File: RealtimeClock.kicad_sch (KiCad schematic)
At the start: 6 parts, among them U21 74HC02, U22 DS12885+, Y2 32.768kHz

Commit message: Schematic cleanup
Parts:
- removed unit 5 of U21
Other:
- moved on the sheet: U21A, U21B, U21C

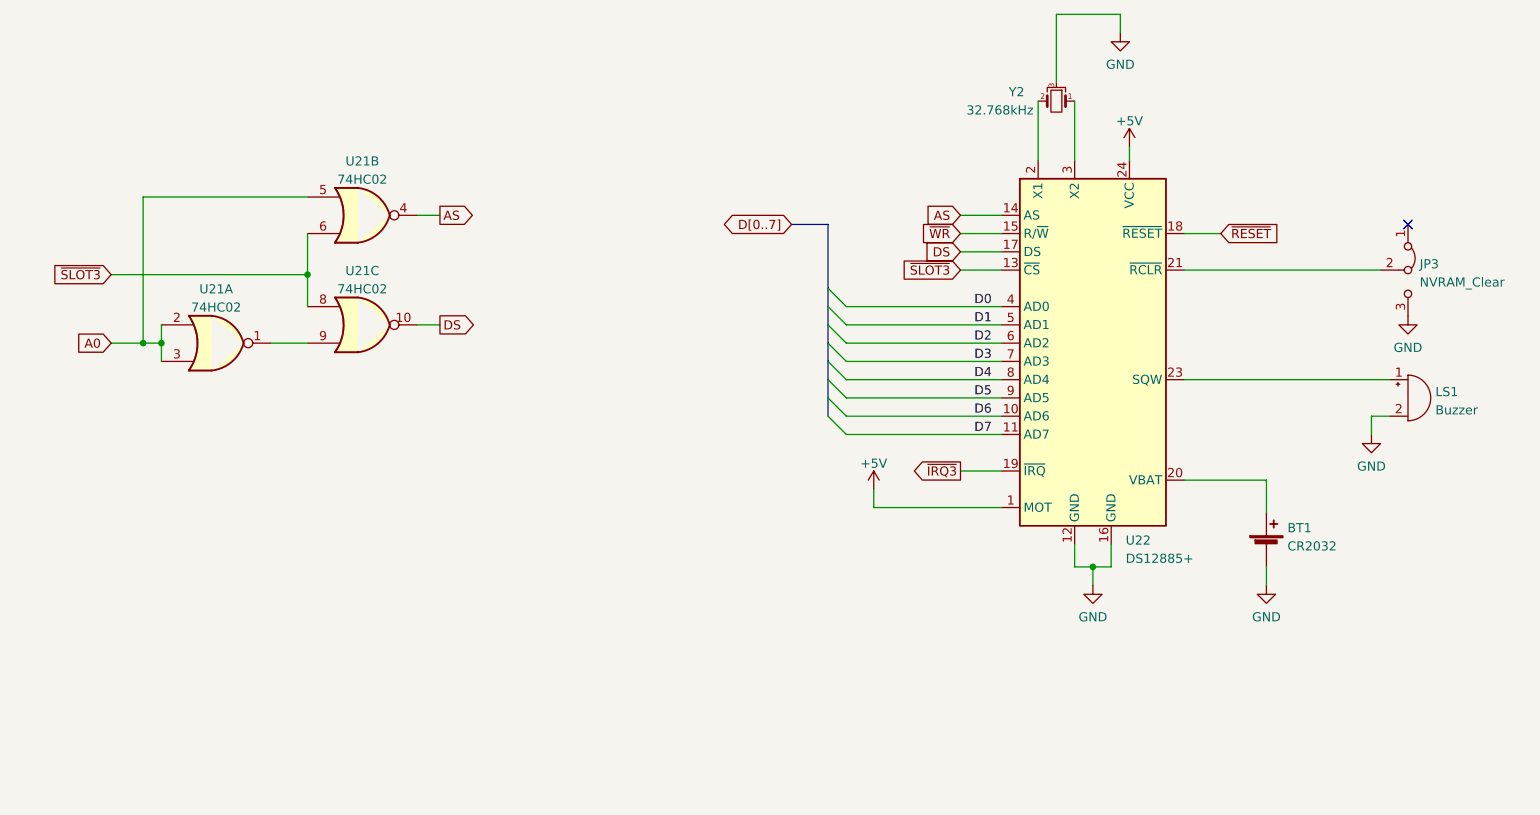
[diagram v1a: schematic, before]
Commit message: Memory expansion moved to low memory
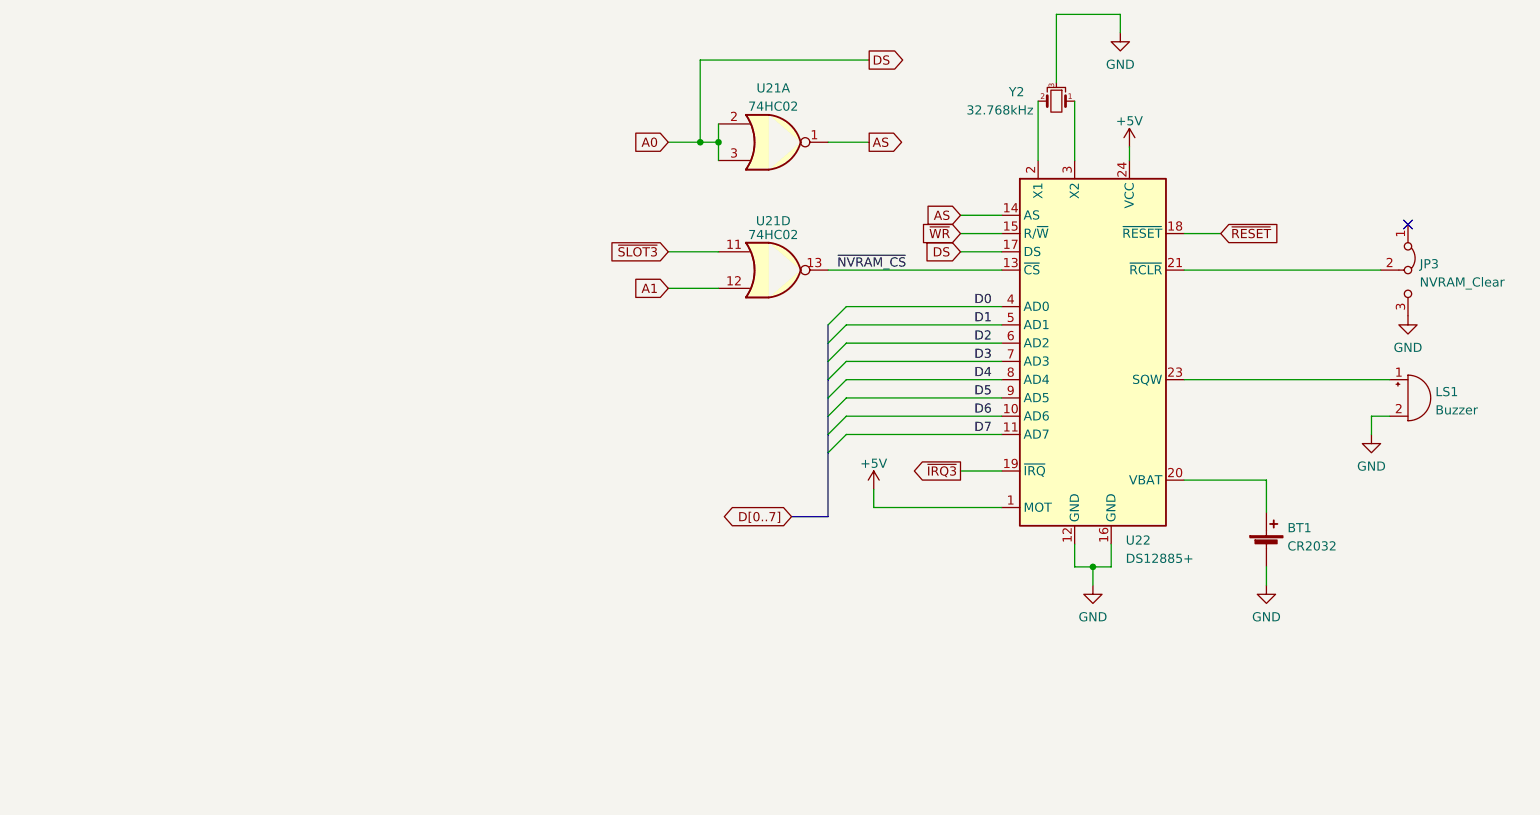
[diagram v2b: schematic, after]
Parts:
- removed unit 3 of U21
- removed unit 2 of U21
- added unit 4 of U21
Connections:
- net DS is gone; now on net A0: U22.17 (DS)
- net AS: now also U21.1
- net ~{SLOT3}: now also U21.11; no longer U22.13 (~{CS})
- new net A1: U21.12
- new net ~{NVRAM_CS}: U21.13, U22.13 (~{CS})
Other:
- moved on the sheet: U21A

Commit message: Misc Updates/Cleanup
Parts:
- U21: value 74HC02 -> 74HCT02
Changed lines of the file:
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@@
       (effects (font (size 1.27 1.27)))
     )
-    (property "Value" "74HC02" (at 144.78 62.9721 0)
+    (property "Value" "74HCT02" (at 144.78 62.9721 0)
       (effects (font (size 1.27 1.27)))
     )
@@
       (effects (font (size 1.27 1.27)))
     )
-    (property "Value" "74HC02" (at 144.78 80.8261 0)
-      (effects (font (size 1.27 1.27)))
-    )
+    (property "Value" "74HCT02" (at 144.78 80.8261 0)
+      (effects (font (size 1.27 1.27)))
+    )

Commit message: Work-in-progress
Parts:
- removed U21: 74HCT02, Package_DIP:DIP-14_W7.62mm_LongPads, symbol 74xx:74HC02
- added U9: 74HCT04, Package_DIP:DIP-14_W7.62mm, symbol 74xx:74HC04
- U22: footprint Package_DIP:DIP-24_W15.24mm_LongPads -> Package_DIP:DIP-24_W15.24mm
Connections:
- net A0: now also U9.3
- net AS: now also U9.4
- net ~{IRQ3} renamed ~{IRQ0}
- net ~{NVRAM_CS} renamed ~{NVRAM}
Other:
- moved on the sheet: BT1, JP3, LS1, U22, Y2

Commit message: Work in progress
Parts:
- JP3: footprint Connector_PinHeader_2.54mm:PinHeader_1x03_P2.54mm_Vertical -> Connector_PinHeader_2.54mm:PinHeader_1x02_P2.54mm_Vertical; symbol Jumper:Jumper_3_Bridged12 -> Jumper:Jumper_2_Open
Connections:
- net GND: now also JP3.2 (B); no longer JP3.3 (B)
- net at JP3.1 (A): now also U22.21 (~{RCLR})
- no-connect marks 1 -> 0
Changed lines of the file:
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@@
   (junction (at 144.145 133.35) (diameter 0) (color 0 0 0 0)
   )
-  (no_connect (at 187.96 85.725))
   (bus_entry (at 107.315 117.475) (size 2.54 -2.54)
     (stroke (width 0) (type default))
@@
     (stroke (width 0) (type default))
   )
+  (wire (pts (xy 198.755 92.075) (xy 198.755 95.25))
+    (stroke (width 0) (type default))
+  )
   (wire (pts (xy 156.845 86.995) (xy 161.925 86.995))
     (stroke (width 0) (type default))
@@
   )
   (wire (pts (xy 168.275 121.285) (xy 168.275 125.73))
+    (stroke (width 0) (type default))
+  )
+  (wire (pts (xy 194.31 92.075) (xy 198.755 92.075))
     (stroke (width 0) (type default))
   )
@@
     )
   )
-  (symbol (lib_id "Jumper:Jumper_3_Bridged12") (at 187.96 92.075 270) (unit 1)
-    (in_bom yes) (on_board yes) (dnp no) (fields_autoplaced)
-    (property "Reference" "JP3" (at 189.5862 91.2403 90)
-      (effects (font (size 1.27 1.27)) (justify left))
-    )
-    (property "Value" "NVRAM_Clear" (at 189.5862 93.7772 90)
-      (effects (font (size 1.27 1.27)) (justify left))
-    )
-    (property "Footprint" "Connector_PinHeader_2.54mm:PinHeader_1x03_P2.54mm_Vertical" (at 187.96 92.075 0)
-      (effects (font (size 1.27 1.27)) hide)
-    )
-    (property "Datasheet" "~" (at 187.96 92.075 0)
+  (symbol (lib_id "Jumper:Jumper_2_Open") (at 189.23 92.075 0) (unit 1)
+    (in_bom yes) (on_board yes) (dnp no) (fields_autoplaced)
+    (property "Reference" "JP3" (at 189.23 87.4141 0)
+      (effects (font (size 1.27 1.27)))
+    )
+    (property "Value" "NVRAM_Clear" (at 189.23 89.3351 0)
+      (effects (font (size 1.27 1.27)))
+    )
+    (property "Footprint" "Connector_PinHeader_2.54mm:PinHeader_1x02_P2.54mm_Vertical" (at 189.23 92.075 0)
+      (effects (font (size 1.27 1.27)) hide)
+    )
+    (property "Datasheet" "~" (at 189.23 92.075 0)
       (effects (font (size 1.27 1.27)) hide)
     )
     (pin "1")
     (pin "2")
-    (pin "3")
     (instances
       (project "Interis 64"
@@
     )
   )
-  (symbol (lib_id "power:GND") (at 187.96 98.425 0) (unit 1)
-    (in_bom yes) (on_board yes) (dnp no) (fields_autoplaced)
-    (property "Reference" "#PWR07" (at 187.96 104.775 0)
-      (effects (font (size 1.27 1.27)) hide)
-    )
-    (property "Value" "GND" (at 187.96 102.8684 0)
-      (effects (font (size 1.27 1.27)))
-    )
-    (property "Footprint" "" (at 187.96 98.425 0)
-      (effects (font (size 1.27 1.27)) hide)
-    )
-    (property "Datasheet" "" (at 187.96 98.425 0)
-      (effects (font (size 1.27 1.27)) hide)
-    )
+  (symbol (lib_id "power:GND") (at 198.755 95.25 0) (unit 1)
+    (in_bom yes) (on_board yes) (dnp no) (fields_autoplaced)
+    (property "Reference" "#PWR07" (at 198.755 101.6 0)
+      (effects (font (size 1.27 1.27)) hide)
+    )
+    (property "Value" "GND" (at 198.755 99.6934 0)
+      (effects (font (size 1.27 1.27)))
+    )
+    (property "Footprint" "" (at 198.755 95.25 0)
+      (effects (font (size 1.27 1.27)) hide)
+    )
+    (property "Datasheet" "" (at 198.755 95.25 0)
+      (effects (font (size 1.27 1.27)) hide)
+    )
